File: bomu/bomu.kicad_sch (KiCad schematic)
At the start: 37 parts, among them U1 NRF52840-CKAA-R7

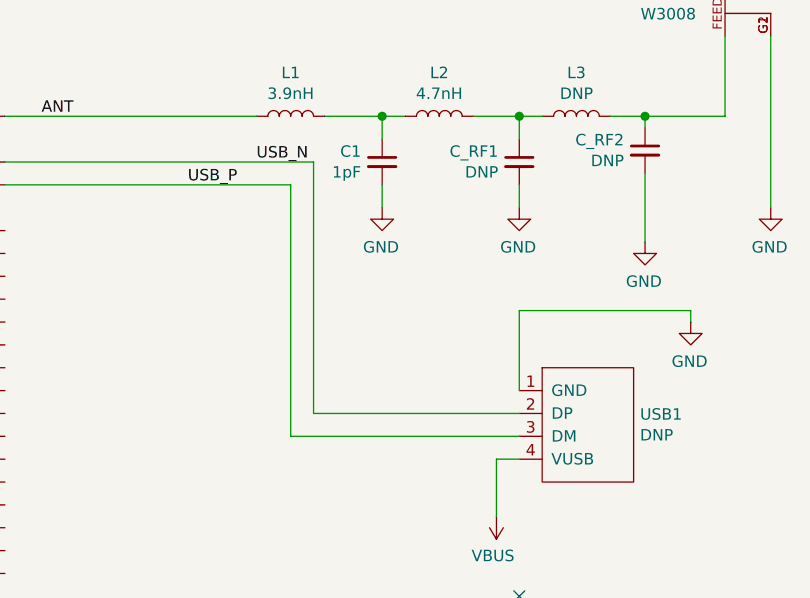
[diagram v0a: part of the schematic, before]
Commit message: Addressing two (2) defects found in 1.0.0, reducing the amount of excess ground layer stitching, and addressing swapped USB data pins (corrected in 1.0.1)
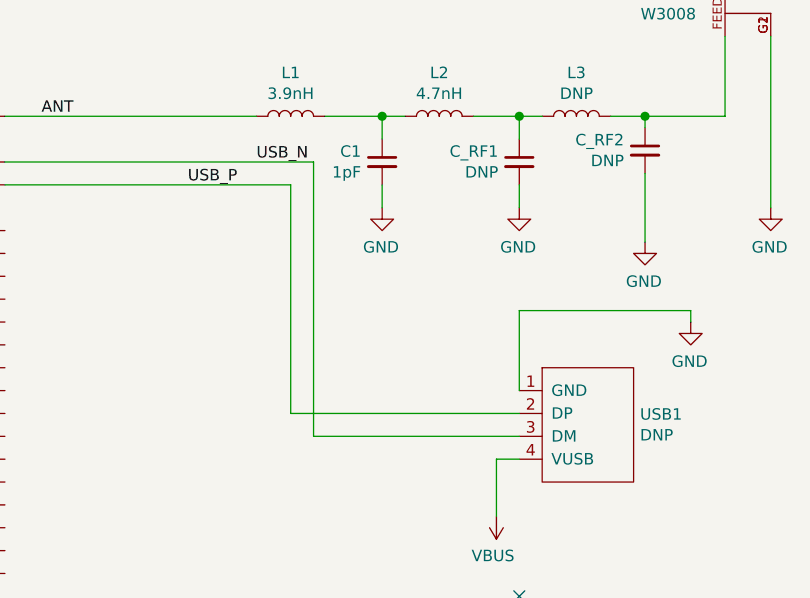
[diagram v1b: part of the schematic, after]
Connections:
- net USB_N: now also USB1.3 (DM); no longer USB1.2 (DP)
- net USB_P: now also USB1.2 (DP); no longer USB1.3 (DM)
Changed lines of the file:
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@@
-    (stroke (width 0) (type solid) (color 0 0 0 0))
-  )
-  (wire (pts (xy 217.17 78.74) (xy 217.17 106.68))
     (stroke (width 0) (type solid) (color 0 0 0 0))
   )
@@
     (stroke (width 0) (type solid) (color 0 0 0 0))
   )
-  (wire (pts (xy 219.71 76.2) (xy 219.71 104.14))
+  (wire (pts (xy 219.71 76.2) (xy 219.71 106.68))
     (stroke (width 0) (type solid) (color 0 0 0 0))
   )
@@
     (stroke (width 0) (type solid) (color 0 0 0 0))
   )
+  (wire (pts (xy 217.17 78.74) (xy 217.17 104.14))
+    (stroke (width 0) (type default) (color 0 0 0 0))
+  )
   (wire (pts (xy 68.58 63.5) (xy 68.58 73.66))
     (stroke (width 0) (type solid) (color 0 0 0 0))
@@
     (stroke (width 0) (type solid) (color 0 0 0 0))
   )
-  (wire (pts (xy 217.17 106.68) (xy 242.57 106.68))
-    (stroke (width 0) (type solid) (color 0 0 0 0))
-  )
   (wire (pts (xy 96.52 160.02) (xy 111.76 160.02))
     (stroke (width 0) (type solid) (color 0 0 0 0))
@@
     (stroke (width 0) (type solid) (color 0 0 0 0))
   )
+  (wire (pts (xy 219.71 106.68) (xy 242.57 106.68))
+    (stroke (width 0) (type default) (color 0 0 0 0))
+  )
   (wire (pts (xy 22.86 114.3) (xy 22.86 119.38))
     (stroke (width 0) (type solid) (color 0 0 0 0))
@@
     (stroke (width 0) (type solid) (color 0 0 0 0))
   )
+  (wire (pts (xy 217.17 104.14) (xy 242.57 104.14))
+    (stroke (width 0) (type default) (color 0 0 0 0))
+  )
   (wire (pts (xy 195.58 35.56) (xy 224.79 35.56))
     (stroke (width 0) (type solid) (color 0 0 0 0))
@@
     (stroke (width 0) (type solid) (color 0 0 0 0))
   )
-  (wire (pts (xy 219.71 104.14) (xy 242.57 104.14))
-    (stroke (width 0) (type solid) (color 0 0 0 0))
-  )

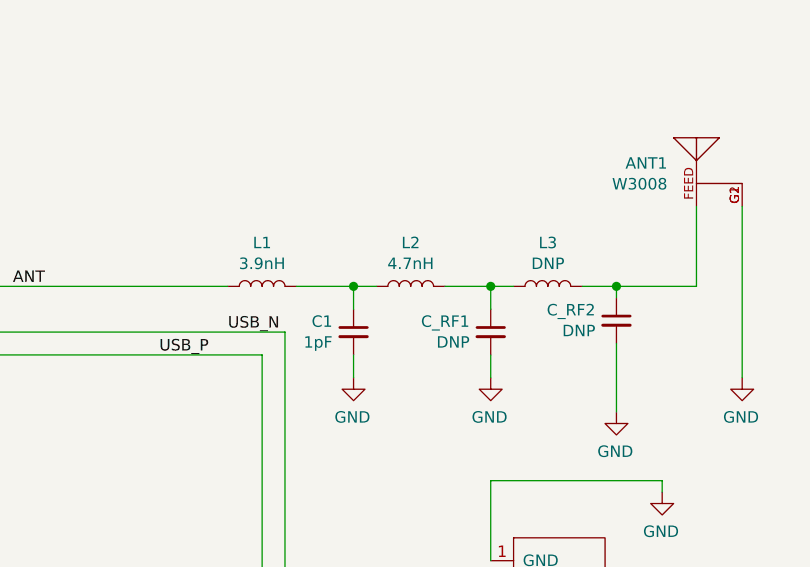
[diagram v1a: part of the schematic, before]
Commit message: Upgrading for KiCAD 7.x format. Adding PDF of bomu-programmer PCB
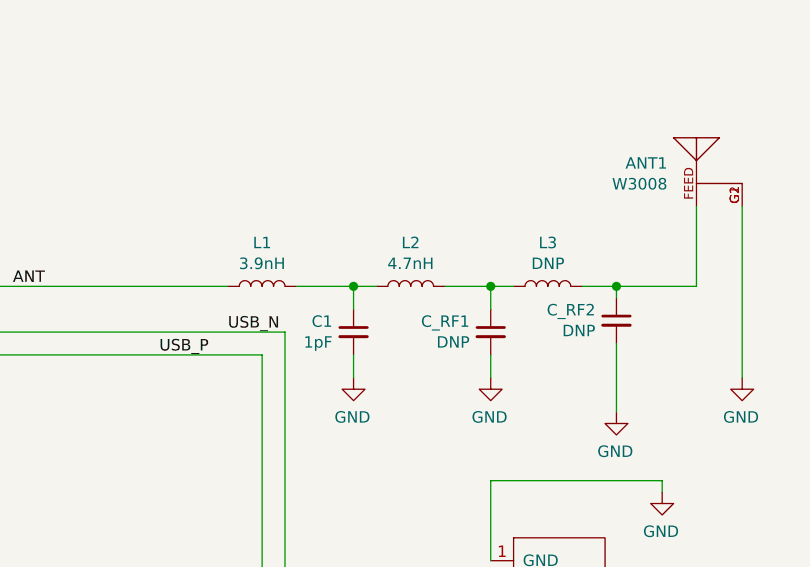
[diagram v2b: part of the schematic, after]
